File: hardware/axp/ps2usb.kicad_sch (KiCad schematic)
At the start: 23 parts, among them J1 DIN8, J2 USB1035, J3 DIN8, J4 DB9_Female_MountingHoles, J5 Conn_01x03_Pin, U1 CH559L-less, U2 MAX232

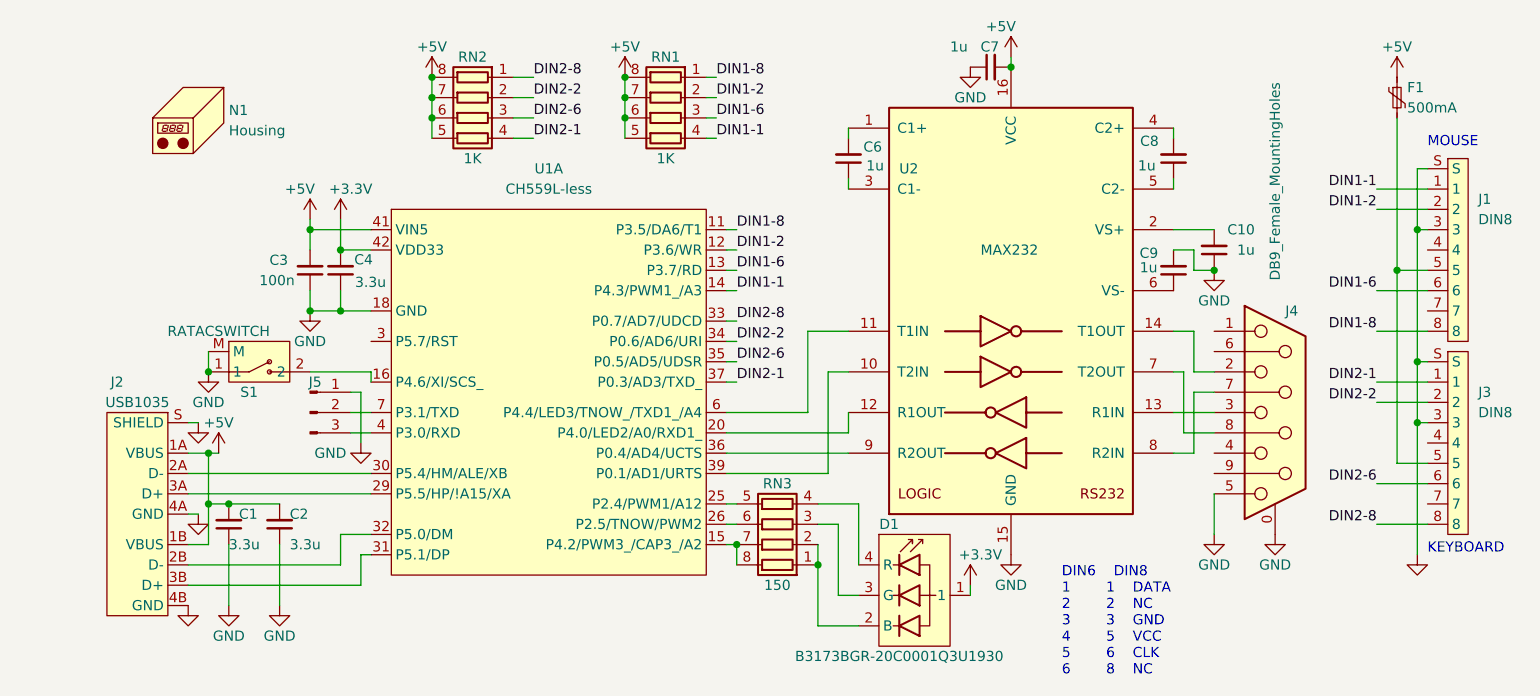
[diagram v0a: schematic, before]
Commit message: Added crystal to PCB
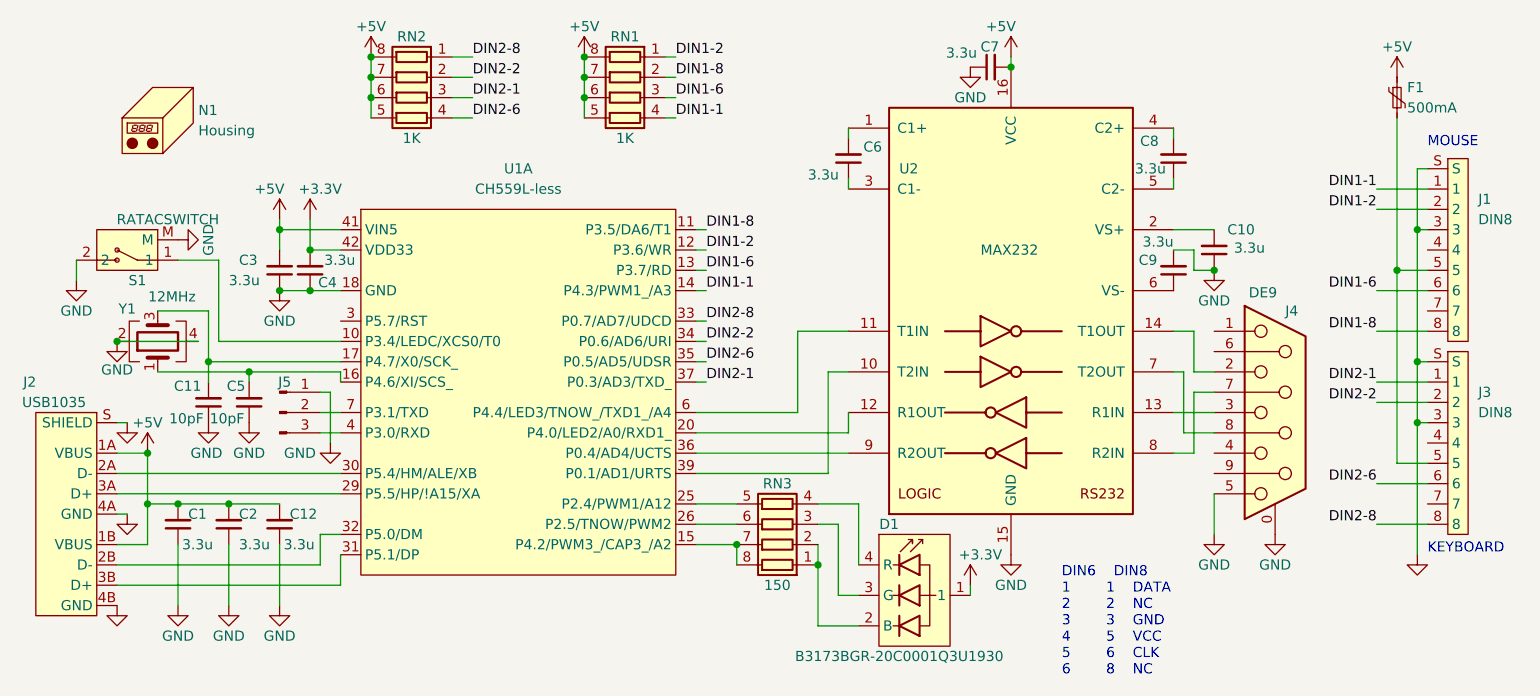
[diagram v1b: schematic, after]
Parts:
- added C11, C5: 10pF, Capacitor_SMD:C_0603_1608Metric, symbol Device:C_Small
- added C12: 3.3u, Capacitor_SMD:C_0603_1608Metric, symbol Device:C_Small
- added Y1: 12MHz, Crystal:Crystal_SMD_3225-4Pin_3.2x2.5mm, symbol Device:Crystal_GND24
- C10, C6, C7, C8, C9: value 1u -> 3.3u
- C3: value 100n -> 3.3u
- J4: value DB9_Female_MountingHoles -> DE9
- RN1, RN2, RN3: footprint Resistor_SMD:R_Array_Convex_4x1206 -> Resistor_SMD:R_Array_Convex_4x0603
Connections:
- net +5V: now also C12.2
- net DIN1-2: now also RN1.1 (R1.1); no longer RN1.2 (R2.1)
- net DIN1-8: now also RN1.2 (R2.1); no longer RN1.1 (R1.1)
- net DIN2-1: now also RN2.3 (R3.1); no longer RN2.4 (R4.1)
- net DIN2-6: now also RN2.4 (R4.1); no longer RN2.3 (R3.1)
- net GND: now also S1.2, C11.1, C12.1, C5.1, Y1.2, Y1.4; no longer S1.1
- net at U1.16 (P4.6/XI/SCS_): now also C5.2, Y1.1; no longer S1.2
- new net: C11.2, U1.17 (P4.7/X0/SCK_), Y1.3
- new net: S1.1, U1.10 (P3.4/LEDC/XCS0/T0)
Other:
- moved on the sheet: C1, C2, C3, C4, J2, J5, N1, RN1, RN2, S1
